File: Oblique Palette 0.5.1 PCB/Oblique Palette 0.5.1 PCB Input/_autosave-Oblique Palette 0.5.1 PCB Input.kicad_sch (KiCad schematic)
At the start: 19 parts, among them J15 Conn_01x03_Male_Pin, J16 Conn_01x03_Female_Pin, J17 AudioJack2_SwitchT, U3 MCP6004

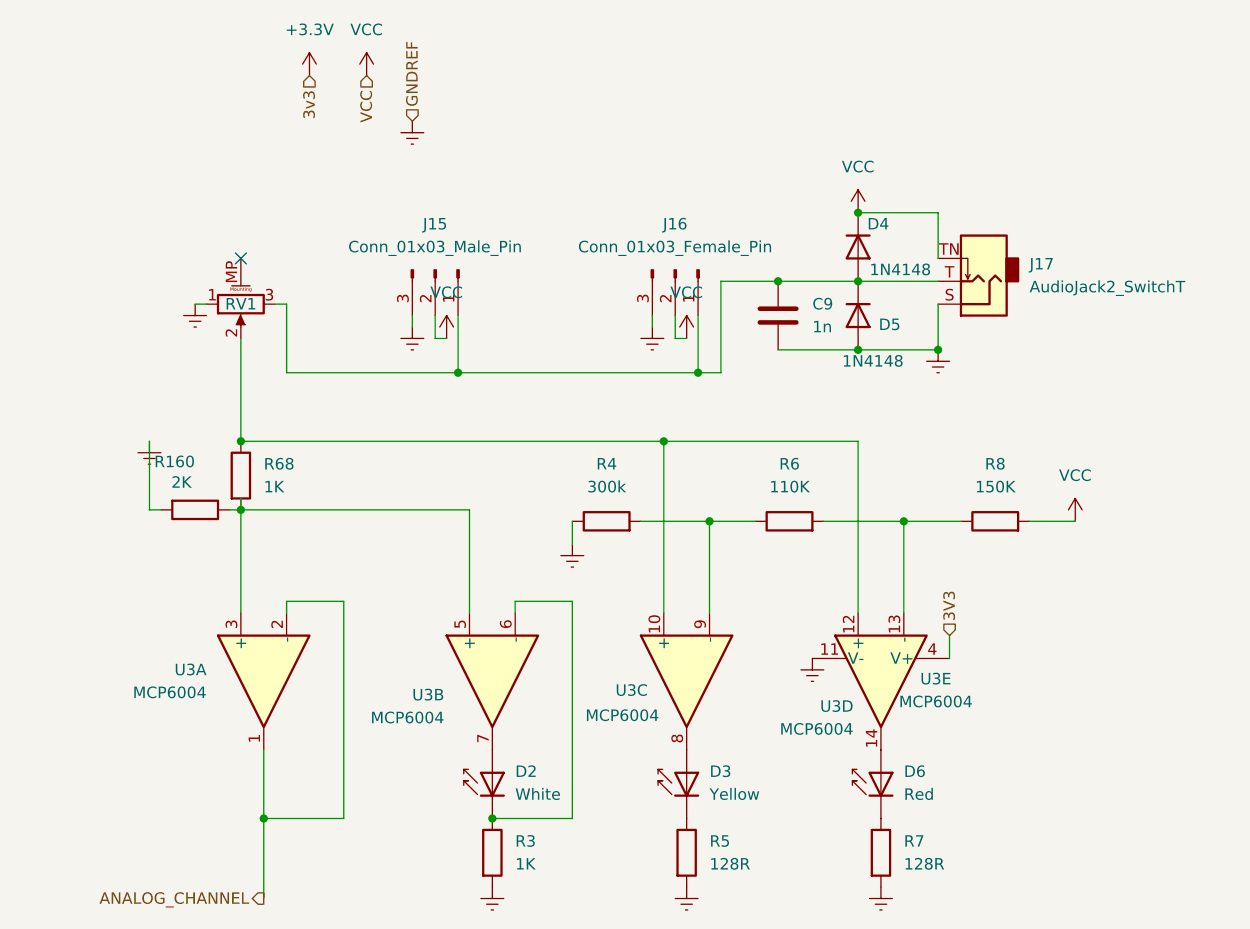
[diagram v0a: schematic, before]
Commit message: All traces(?) now connected on PCB.
This is looking good to me. Vcc and VServo are merged for simplicity. Not the best solution. I think maybe a breakable trace or a single jumper might be the way to do this.
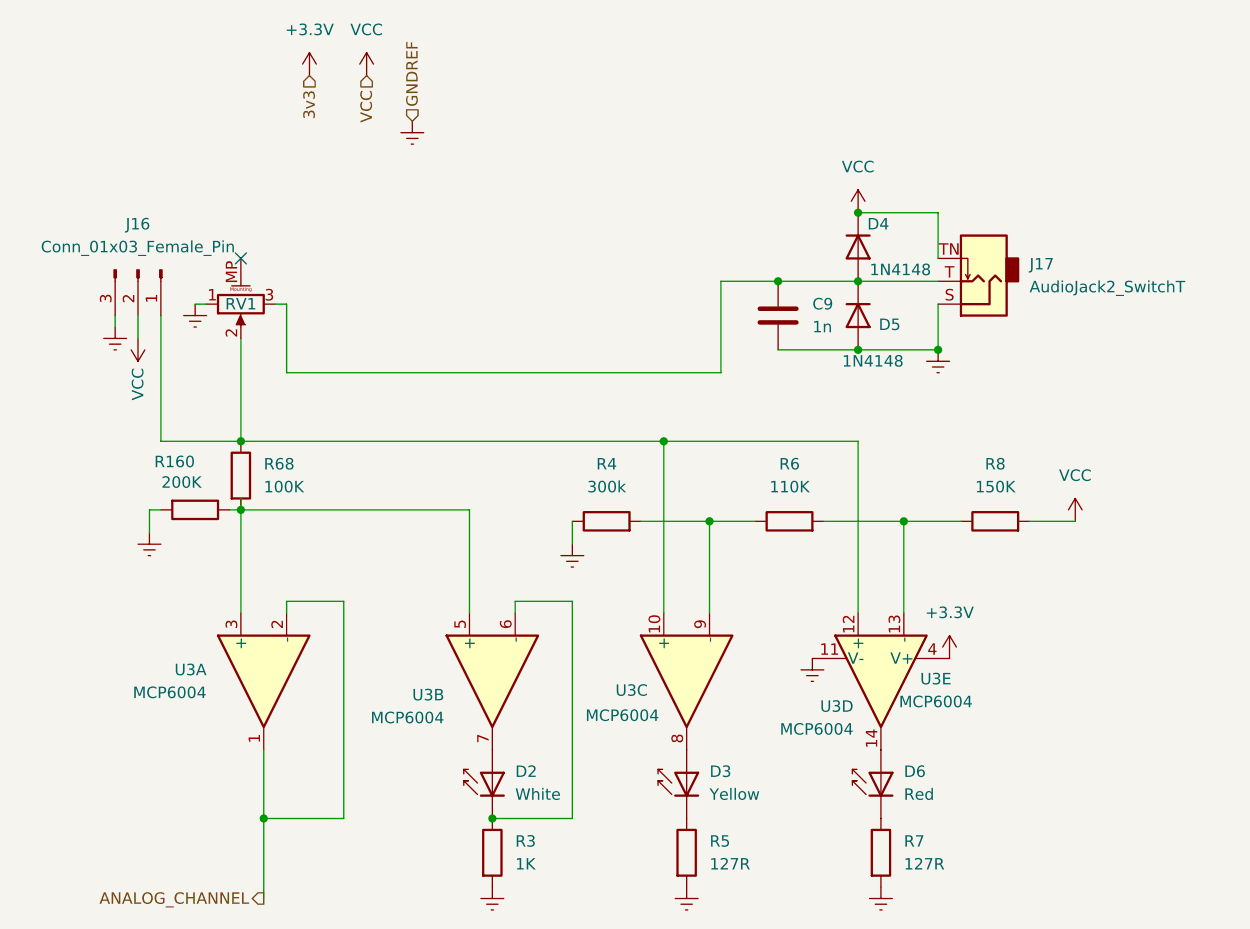
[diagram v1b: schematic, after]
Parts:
- removed J15: Conn_01x03_Male_Pin, Connector_PinHeader_2.54mm:PinHeader_1x03_P2.54mm_Vertical, symbol Connector:Conn_01x03_Pin
- R160: value 2K -> 200K
- R5, R7: value 128R -> 127R
- R68: value 1K -> 100K
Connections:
- net 3V3 is gone; now on net +3.3V: U3.4 (V+)
- net at C9.1, D4.2 (A), D5.1 (K)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: no longer J16.1 (Pin_1)
- net at R68.1, RV1.2, U3.10 (+)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: now also J16.1 (Pin_1)
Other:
- moved on the sheet: J16
